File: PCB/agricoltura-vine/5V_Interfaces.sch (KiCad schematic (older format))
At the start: 16 parts, among them T19 TSW-108-07-G-T, T20 TSW-108-07-G-T, U10 MCP23017T-E_ML, U8 SN74LV541APWR, U9 TXB0108PWR

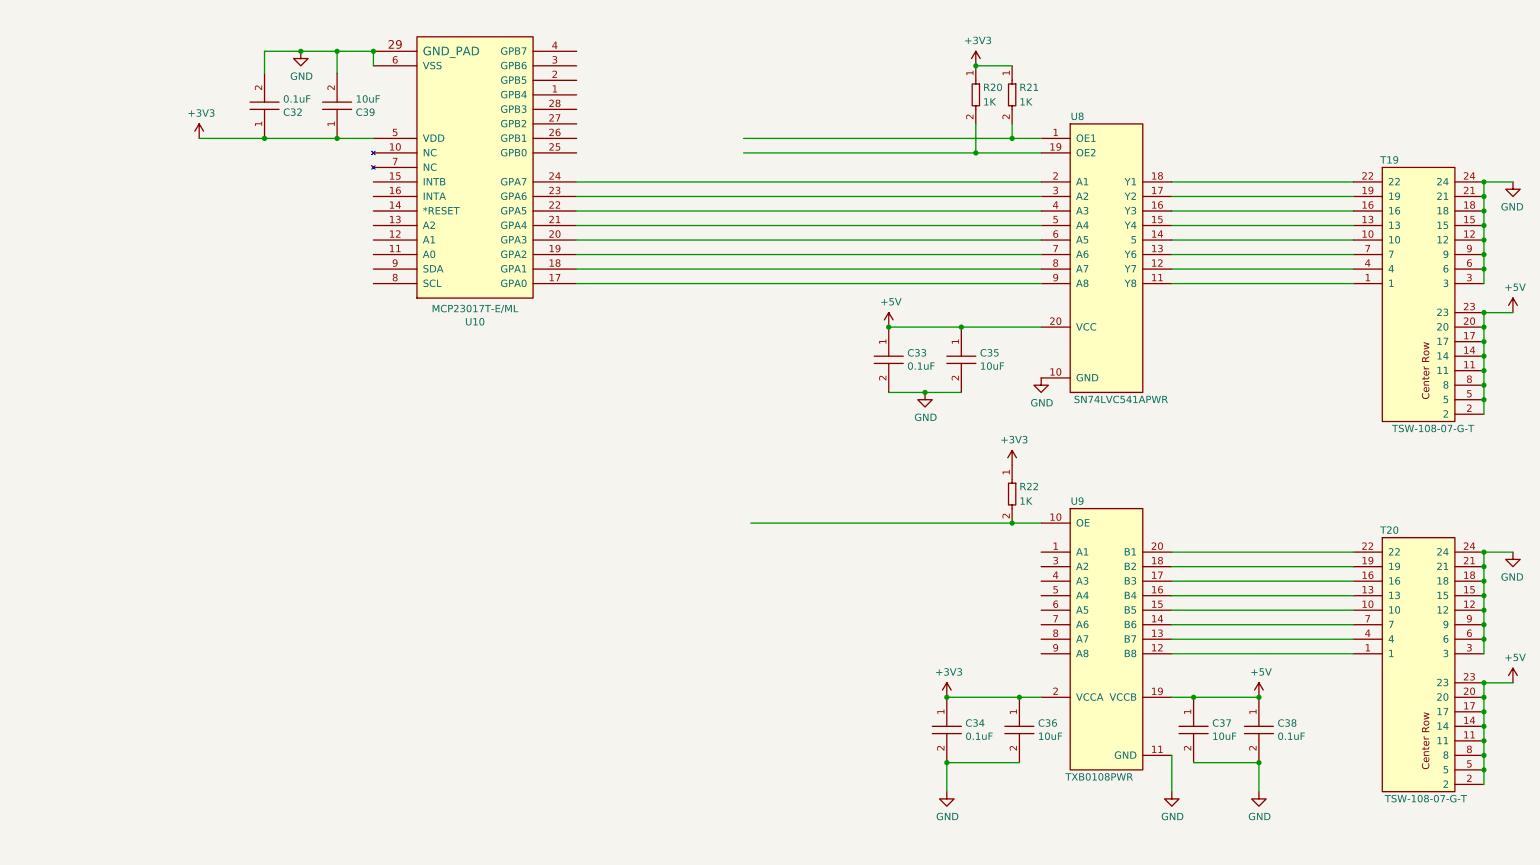
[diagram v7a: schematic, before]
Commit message: Big Update
Dropped 8 5V outputs in favor of two relays. Ditched microchip IO expander for a Ti one that does level conversion for outputs, eliminates Ti bidriectional converter and 74 line driver from design, simplifying everything.
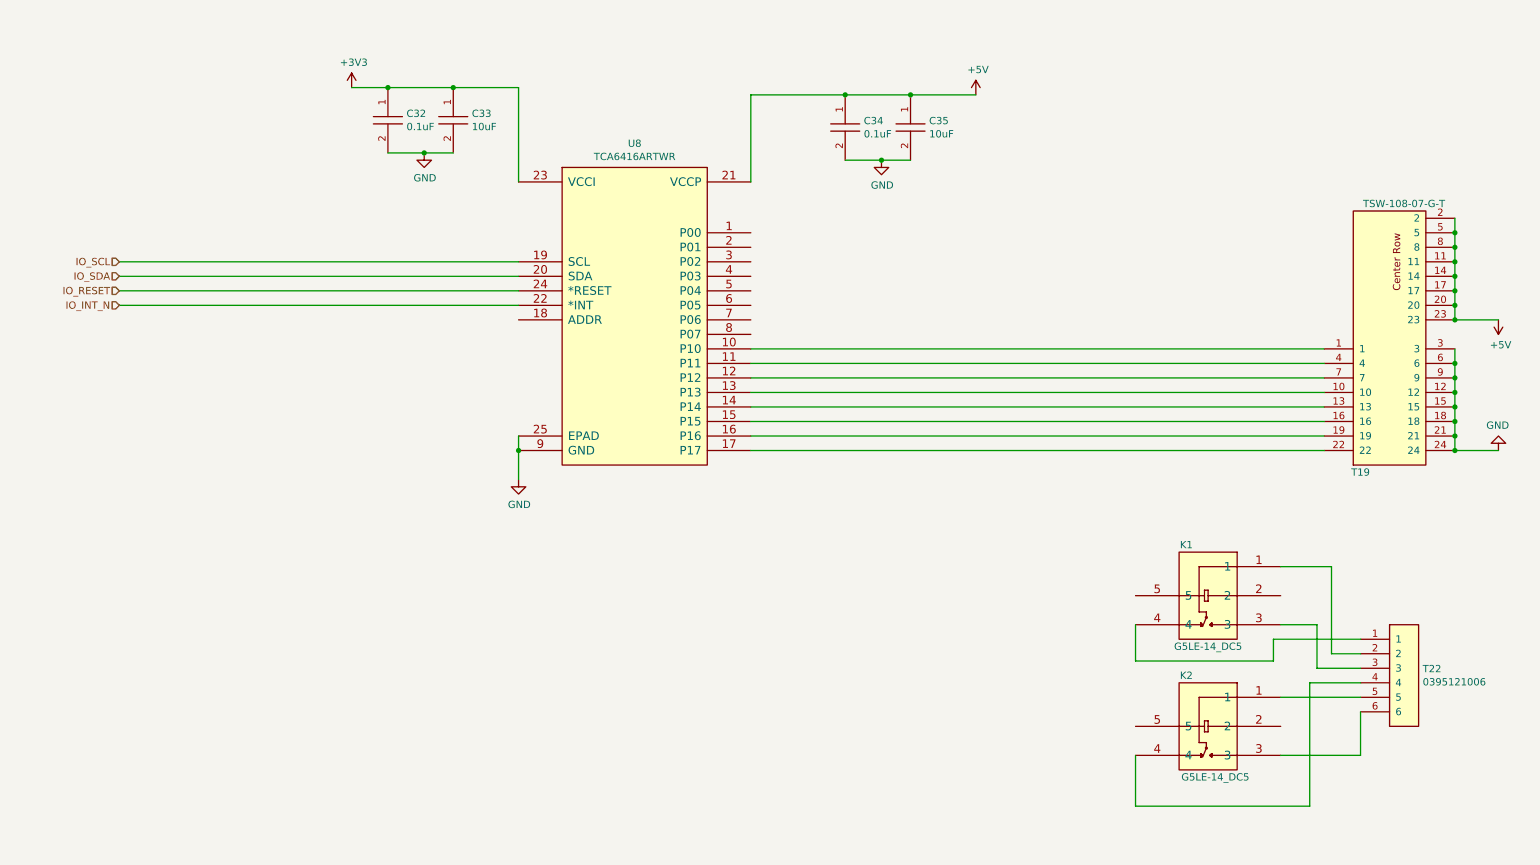
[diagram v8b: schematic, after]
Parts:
- removed C33, C38: C0402C104K9PACTU, AVR-KiCAD-Lib-Resistors:R0402, symbol AVR-KiCAD-Lib-Capacitors:C0402C104K9PACTU
- removed C36, C37, C39: GRM188R61A106KE69J, AVR-KiCAD-Lib-Capacitors:C0603, symbol AVR-KiCAD-Lib-Capacitors:GRM188R61A106KE69J
- removed R20, R21, R22: RC0402FR-071KL, AVR-KiCAD-Lib-Resistors:R0402, symbol AVR-KiCAD-Lib-Resistors:RC0402FR-071KL
- removed T20: TSW-108-07-G-T, AVR-KiCAD-Lib-Connectors:TSW-108-07-G-T, symbol AVR-KiCAD-Lib-Connectors:TSW-108-07-G-T
- removed U10: MCP23017T-E_ML, AVR-KiCAD-Lib-ICs:MCP23017T-E, symbol AVR-KiCAD-Lib-ICs:MCP23017T-E_ML
- removed U8: SN74LV541APWR, AVR-KiCAD-Lib-ICs:SN74LVC541APWR, symbol AVR-KiCAD-Lib-ICs:SN74LV541APWR
- removed U9: TXB0108PWR, AVR-KiCAD-Lib-ICs:TXB0108PWR, symbol AVR-KiCAD-Lib-ICs:TXB0108PWR
- added C33: GRM188R61A106KE69J, AVR-KiCAD-Lib-Capacitors:C0603, symbol AVR-KiCAD-Lib-Capacitors:GRM188R61A106KE69J
- added K1, K2: G5LE-14_DC5, AVR-KiCAD-Lib-Relays-Contactors:G5LE-14_DC5, symbol AVR-KiCAD-Lib-Mech-Relays-Contactors:G5LE-14_DC5
- added T22: 0395121006, AVR-KiCAD-Lib-Connectors:0395121006, symbol AVR-KiCAD-Lib-Connectors:0395121006
- added U8: TCA6416ARTWR, AVR-KiCAD-Lib-ICs:TCA6416ARTWR, symbol AVR-KiCAD-Lib-ICs:TCA6416ARTWR
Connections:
- net labels added: IO_INT_N, IO_RESET, IO_SCL, IO_SDA
- wire segments 87 -> 59
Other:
- moved on the sheet: T19
